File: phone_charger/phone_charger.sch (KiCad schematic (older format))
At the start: 19 parts, among them J1 Conn_01x02, J2 UE27AC54100, U1 ADP2302

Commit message: Place USB on grid; connect shield
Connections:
- wire segments 47 -> 50
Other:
- moved on the sheet: J2
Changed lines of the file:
@@
 L phone_charger-rescue:UE27AC54100-dk_USB-DVI-HDMI-Connectors J2
 U 1 1 5B88DA27
-P 6700 4750
-F 0 "J2" H 6597 4690 60  0000 R CNN
-F 1 "UE27AC54100" H 6597 4796 60  0000 R CNN
-F 2 "phone_charger:USB_A_Female_SS-52100-001" H 6900 4950 60  0001 L CNN
-F 3 "https://www.amphenolcanada.com/ProductSearch/drawings/AC/UE27ACX4X0X.pdf" H 6900 5050 60  0001 L CNN
-F 4 "UE27AC54100-ND" H 6900 5150 60  0001 L CNN "Digi-Key_PN"
-F 5 "UE27AC54100" H 6900 5250 60  0001 L CNN "MPN"
-F 6 "Connectors, Interconnects" H 6900 5350 60  0001 L CNN "Category"
-F 7 "USB, DVI, HDMI Connectors" H 6900 5450 60  0001 L CNN "Family"
-F 8 "https://www.amphenolcanada.com/ProductSearch/drawings/AC/UE27ACX4X0X.pdf" H 6900 5550 60  0001 L CNN "DK_Datasheet_Link"
-F 9 "/product-detail/en/amphenol-commercial-products/UE27AC54100/UE27AC54100-ND/1972253" H 6900 5650 60  0001 L CNN "DK_Detail_Page"
-F 10 "CONN RCPT USB TYPE A R/A GOLD" H 6900 5750 60  0001 L CNN "Description"
-F 11 "Amphenol Commercial Products" H 6900 5850 60  0001 L CNN "Manufacturer"
-F 12 "Active" H 6900 5950 60  0001 L CNN "Status"
-	1    6700 4750
+P 6600 4700
+F 0 "J2" H 6497 4640 60  0000 R CNN
+F 1 "UE27AC54100" H 6497 4746 60  0000 R CNN
+F 2 "phone_charger:USB_A_Female_SS-52100-001" H 6800 4900 60  0001 L CNN
+F 3 "https://www.amphenolcanada.com/ProductSearch/drawings/AC/UE27ACX4X0X.pdf" H 6800 5000 60  0001 L CNN
+F 4 "UE27AC54100-ND" H 6800 5100 60  0001 L CNN "Digi-Key_PN"
+F 5 "UE27AC54100" H 6800 5200 60  0001 L CNN "MPN"
+F 6 "Connectors, Interconnects" H 6800 5300 60  0001 L CNN "Category"
+F 7 "USB, DVI, HDMI Connectors" H 6800 5400 60  0001 L CNN "Family"
+F 8 "https://www.amphenolcanada.com/ProductSearch/drawings/AC/UE27ACX4X0X.pdf" H 6800 5500 60  0001 L CNN "DK_Datasheet_Link"
+F 9 "/product-detail/en/amphenol-commercial-products/UE27AC54100/UE27AC54100-ND/1972253" H 6800 5600 60  0001 L CNN "DK_Detail_Page"
+F 10 "CONN RCPT USB TYPE A R/A GOLD" H 6800 5700 60  0001 L CNN "Description"
+F 11 "Amphenol Commercial Products" H 6800 5800 60  0001 L CNN "Manufacturer"
+F 12 "Active" H 6800 5900 60  0001 L CNN "Status"
+	1    6600 4700
 	-1   0    0    1
 $EndComp
@@
 L phone_charger-rescue:R-Device R3
 U 1 1 5B88DF7C
-P 5500 4000
-F 0 "R3" H 5570 4046 50  0000 L CNN
-F 1 "75k" H 5570 3955 50  0000 L CNN
-F 2 "Resistors_SMD:R_0805_HandSoldering" V 5430 4000 50  0001 C CNN
-F 3 "~" H 5500 4000 50  0001 C CNN
-	1    5500 4000
+P 5400 3950
+F 0 "R3" H 5470 3996 50  0000 L CNN
+F 1 "75k" H 5470 3905 50  0000 L CNN
+F 2 "Resistors_SMD:R_0805_HandSoldering" V 5330 3950 50  0001 C CNN
+F 3 "~" H 5400 3950 50  0001 C CNN
+	1    5400 3950
 	1    0    0    -1
 $EndComp
@@
 L phone_charger-rescue:R-Device R4
 U 1 1 5B88E002
-P 5500 4500
-F 0 "R4" H 5570 4546 50  0000 L CNN
-F 1 "50k" H 5570 4455 50  0000 L CNN
-F 2 "Resistors_SMD:R_0805_HandSoldering" V 5430 4500 50  0001 C CNN
-F 3 "~" H 5500 4500 50  0001 C CNN
-	1    5500 4500
+P 5400 4450
+F 0 "R4" H 5470 4496 50  0000 L CNN
+F 1 "50k" H 5470 4405 50  0000 L CNN
+F 2 "Resistors_SMD:R_0805_HandSoldering" V 5330 4450 50  0001 C CNN
+F 3 "~" H 5400 4450 50  0001 C CNN
+	1    5400 4450
 	1    0    0    -1
 $EndComp
@@
 L phone_charger-rescue:VBUS-power #PWR05
 U 1 1 5B88E11B
-P 5500 3850
-F 0 "#PWR05" H 5500 3700 50  0001 C CNN
-F 1 "VBUS" H 5515 4023 50  0000 C CNN
-F 2 "" H 5500 3850 50  0001 C CNN
-F 3 "" H 5500 3850 50  0001 C CNN
-	1    5500 3850
+P 5400 3800
+F 0 "#PWR05" H 5400 3650 50  0001 C CNN
+F 1 "VBUS" H 5415 3973 50  0000 C CNN
+F 2 "" H 5400 3800 50  0001 C CNN
+F 3 "" H 5400 3800 50  0001 C CNN
+	1    5400 3800
 	1    0    0    -1
 $EndComp
@@
 L phone_charger-rescue:GND-power #PWR06
 U 1 1 5B88E140
-P 5500 4650
-F 0 "#PWR06" H 5500 4400 50  0001 C CNN
-F 1 "GND" H 5505 4477 50  0000 C CNN
-F 2 "" H 5500 4650 50  0001 C CNN
-F 3 "" H 5500 4650 50  0001 C CNN
-	1    5500 4650
+P 5400 4600
+F 0 "#PWR06" H 5400 4350 50  0001 C CNN
+F 1 "GND" H 5405 4427 50  0000 C CNN
+F 2 "" H 5400 4600 50  0001 C CNN
+F 3 "" H 5400 4600 50  0001 C CNN
+	1    5400 4600
 	1    0    0    -1
 $EndComp
@@
 L phone_charger-rescue:R-Device R5
 U 1 1 5B88ED75
-P 5500 5300
-F 0 "R5" H 5570 5346 50  0000 L CNN
-F 1 "43k" H 5570 5255 50  0000 L CNN
-F 2 "Resistors_SMD:R_0603_HandSoldering" V 5430 5300 50  0001 C CNN
-F 3 "~" H 5500 5300 50  0001 C CNN
-	1    5500 5300
+P 5400 5250
+F 0 "R5" H 5470 5296 50  0000 L CNN
+F 1 "43k" H 5470 5205 50  0000 L CNN
+F 2 "Resistors_SMD:R_0603_HandSoldering" V 5330 5250 50  0001 C CNN
+F 3 "~" H 5400 5250 50  0001 C CNN
+	1    5400 5250
 	1    0    0    -1
 $EndComp
@@
 L phone_charger-rescue:R-Device R6
 U 1 1 5B88ED7B
-P 5500 5800
-F 0 "R6" H 5570 5846 50  0000 L CNN
-F 1 "50k" H 5570 5755 50  0000 L CNN
-F 2 "Resistors_SMD:R_0805_HandSoldering" V 5430 5800 50  0001 C CNN
-F 3 "~" H 5500 5800 50  0001 C CNN
-	1    5500 5800
+P 5400 5750
+F 0 "R6" H 5470 5796 50  0000 L CNN
+F 1 "50k" H 5470 5705 50  0000 L CNN
+F 2 "Resistors_SMD:R_0805_HandSoldering" V 5330 5750 50  0001 C CNN
+F 3 "~" H 5400 5750 50  0001 C CNN
+	1    5400 5750
 	1    0    0    -1
 $EndComp
@@
 L phone_charger-rescue:VBUS-power #PWR07
 U 1 1 5B88ED81
-P 5500 5150
-F 0 "#PWR07" H 5500 5000 50  0001 C CNN
-F 1 "VBUS" H 5515 5323 50  0000 C CNN
-F 2 "" H 5500 5150 50  0001 C CNN
-F 3 "" H 5500 5150 50  0001 C CNN
-	1    5500 5150
+P 5400 5100
+F 0 "#PWR07" H 5400 4950 50  0001 C CNN
+F 1 "VBUS" H 5415 5273 50  0000 C CNN
+F 2 "" H 5400 5100 50  0001 C CNN
+F 3 "" H 5400 5100 50  0001 C CNN
+	1    5400 5100
 	1    0    0    -1
 $EndComp
@@
 L phone_charger-rescue:GND-power #PWR08
 U 1 1 5B88ED87
-P 5500 5950
-F 0 "#PWR08" H 5500 5700 50  0001 C CNN
-F 1 "GND" H 5505 5777 50  0000 C CNN
-F 2 "" H 5500 5950 50  0001 C CNN
-F 3 "" H 5500 5950 50  0001 C CNN
-	1    5500 5950
+P 5400 5900
+F 0 "#PWR08" H 5400 5650 50  0001 C CNN
+F 1 "GND" H 5405 5727 50  0000 C CNN
+F 2 "" H 5400 5900 50  0001 C CNN
+F 3 "" H 5400 5900 50  0001 C CNN
+	1    5400 5900
 	1    0    0    -1
 $EndComp
@@
 L phone_charger-rescue:R-Device R7
 U 1 1 5B88F6A0
-P 5800 4800
-F 0 "R7" H 5850 5100 50  0000 L CNN
-F 1 "0R (OPT)" H 5850 5000 50  0000 L CNN
-F 2 "Resistors_SMD:R_0603_HandSoldering" V 5730 4800 50  0001 C CNN
-F 3 "~" H 5800 4800 50  0001 C CNN
-	1    5800 4800
-	1    0    0    -1
-$EndComp
-Wire Wire Line
-	5800 4250 5800 4650
-Connection ~ 5800 4650
-Wire Wire Line
-	5800 5550 5800 4950
-Connection ~ 5800 4950
-Wire Wire Line
-	5500 4150 5500 4250
-Wire Wire Line
-	5500 5450 5500 5550
-Wire Wire Line
-	5800 4250 5500 4250
-Connection ~ 5500 4250
-Wire Wire Line
-	5500 4250 5500 4350
-Wire Wire Line
-	5800 5550 5500 5550
-Connection ~ 5500 5550
-Wire Wire Line
-	5500 5550 5500 5650
+P 5700 4750
+F 0 "R7" H 5750 5050 50  0000 L CNN
+F 1 "0R (OPT)" H 5750 4950 50  0000 L CNN
+F 2 "Resistors_SMD:R_0603_HandSoldering" V 5630 4750 50  0001 C CNN
+F 3 "~" H 5700 4750 50  0001 C CNN
+	1    5700 4750
+	1    0    0    -1
+$EndComp
+Wire Wire Line
+	5700 4200 5700 4600
+Connection ~ 5700 4600
+Wire Wire Line
+	5700 5500 5700 4900
+Connection ~ 5700 4900
+Wire Wire Line
+	5400 4100 5400 4200
+Wire Wire Line
+	5400 5400 5400 5500
+Wire Wire Line
+	5700 4200 5400 4200
+Connection ~ 5400 4200
+Wire Wire Line
+	5400 4200 5400 4300
+Wire Wire Line
+	5700 5500 5400 5500
+Connection ~ 5400 5500
+Wire Wire Line
+	5400 5500 5400 5600
 $Comp
 L phone_charger-rescue:GND-power #PWR011
 U 1 1 5B89256C
-P 6300 5950
-F 0 "#PWR011" H 6300 5700 50  0001 C CNN
-F 1 "GND" H 6305 5777 50  0000 C CNN
-F 2 "" H 6300 5950 50  0001 C CNN
-F 3 "" H 6300 5950 50  0001 C CNN
-	1    6300 5950
-	1    0    0    -1
-$EndComp
-Wire Wire Line
-	6400 4950 6300 4950
+P 6200 5900
+F 0 "#PWR011" H 6200 5650 50  0001 C CNN
+F 1 "GND" H 6205 5727 50  0000 C CNN
+F 2 "" H 6200 5900 50  0001 C CNN
+F 3 "" H 6200 5900 50  0001 C CNN
+	1    6200 5900
+	1    0    0    -1
+$EndComp
+Wire Wire Line
+	6300 4900 6200 4900
 $Comp
 L phone_charger-rescue:VBUS-power #PWR010
 U 1 1 5B892D7D
-P 6300 3850
-F 0 "#PWR010" H 6300 3700 50  0001 C CNN
-F 1 "VBUS" H 6315 4023 50  0000 C CNN
-F 2 "" H 6300 3850 50  0001 C CNN
-F 3 "" H 6300 3850 50  0001 C CNN
-	1    6300 3850
-	1    0    0    -1
-$EndComp
-Wire Wire Line
-	6300 3850 6300 4650
-Wire Wire Line
-	6300 4650 6400 4650
+P 6200 3800
+F 0 "#PWR010" H 6200 3650 50  0001 C CNN
+F 1 "VBUS" H 6215 3973 50  0000 C CNN
+F 2 "" H 6200 3800 50  0001 C CNN
+F 3 "" H 6200 3800 50  0001 C CNN
+	1    6200 3800
+	1    0    0    -1
+$EndComp
+Wire Wire Line
+	6200 3800 6200 4600
+Wire Wire Line
+	6200 4600 6300 4600
 $Comp
 L phone_charger-rescue:Polyfuse-Device F1
@@
 Wire Wire Line
 	8400 1950 8400 1150
-Text Label 6250 4750 0    50   ~ 0
+Text Label 6150 4700 0    50   ~ 0
 D-
-Text Label 6250 4850 0    50   ~ 0
+Text Label 6150 4800 0    50   ~ 0
 D+
 Text Notes 4700 6350 0    50   ~ 0
 Populate EITHER Apple divider resistors or 200 ohm short.
 Wire Wire Line
-	6100 4750 6100 4650
-Wire Wire Line
-	6100 4750 6400 4750
-Wire Wire Line
-	5800 4650 6100 4650
-Wire Wire Line
-	6100 4850 6100 4950
-Wire Wire Line
-	6100 4850 6400 4850
-Wire Wire Line
-	5800 4950 6100 4950
+	6000 4700 6000 4600
+Wire Wire Line
+	6000 4700 6300 4700
+Wire Wire Line
+	5700 4600 6000 4600
+Wire Wire Line
+	6000 4800 6000 4900
+Wire Wire Line
+	6000 4800 6300 4800
+Wire Wire Line
+	5700 4900 6000 4900
 $Comp
 L phone_charger-rescue:ADP2302 U1
@@
 $EndComp
 Wire Wire Line
-	6300 4950 6300 5950
+	6200 4900 6200 5200
+Wire Wire Line
+	6500 5100 6500 5200
+Wire Wire Line
+	6500 5200 6200 5200
+Connection ~ 6200 5200
+Wire Wire Line
+	6200 5200 6200 5900
 $EndSCHEMATC

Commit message: Point to footprint in our library
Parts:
- D2: footprint Diodes_SMD:D_SOD-123 -> phone_charger:D_SOD-123
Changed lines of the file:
@@
 F 0 "D2" H 3550 1384 50  0000 C CNN
 F 1 "D_Schottky" H 3550 1475 50  0000 C CNN
-F 2 "Diodes_SMD:D_SOD-123" H 3550 1600 50  0001 C CNN
+F 2 "phone_charger:D_SOD-123" H 3550 1600 50  0001 C CNN
 F 3 "~" H 3550 1600 50  0001 C CNN
 	1    3550 1600

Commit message: Use smaller THT resistor
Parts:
- R1: footprint Resistors_THT:R_Axial_DIN0309_L9.0mm_D3.2mm_P12.70mm_Horizontal -> Resistor_THT:R_Axial_DIN0207_L6.3mm_D2.5mm_P10.16mm_Horizontal
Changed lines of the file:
@@
 F 0 "R1" H 3070 4596 50  0000 L CNN
 F 1 "300R" H 3070 4505 50  0000 L CNN
-F 2 "Resistors_THT:R_Axial_DIN0309_L9.0mm_D3.2mm_P12.70mm_Horizontal" V 2930 4550 50  0001 C CNN
+F 2 "Resistor_THT:R_Axial_DIN0207_L6.3mm_D2.5mm_P10.16mm_Horizontal" V 2930 4550 50  0001 C CNN
 F 3 "~" H 3000 4550 50  0001 C CNN
 	1    3000 4550

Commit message: Updated header footprint for charger layout
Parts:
- J1: footprint Pin_Headers:Pin_Header_Straight_1x02_Pitch1.00mm -> Pin_Headers:Pin_Header_Straight_1x02_Pitch2.54mm
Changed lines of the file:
@@
 F 0 "J1" H 2120 1817 50  0000 C CNN
 F 1 "Conn_01x02" H 2120 1726 50  0000 C CNN
-F 2 "Pin_Headers:Pin_Header_Straight_1x02_Pitch1.00mm" H 2200 1600 50  0001 C CNN
+F 2 "Pin_Headers:Pin_Header_Straight_1x02_Pitch2.54mm" H 2200 1600 50  0001 C CNN
 F 3 "~" H 2200 1600 50  0001 C CNN
 	1    2200 1600

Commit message: Label switch node
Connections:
- net labels added: SWN
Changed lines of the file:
@@
 Wire Wire Line
 	6200 5200 6200 5900
+Text Label 6950 1950 0    50   ~ 0
+SWN
 $EndSCHEMATC

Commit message: Remap Device libraries and remove unused symbols
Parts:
- C1, C2, C3, C4: symbol phone_charger-rescue:C-device -> Device:C
- D3: symbol phone_charger-rescue:D_Schottky-device -> Device:D_Schottky
- F1: symbol phone_charger-rescue:Polyfuse-Device -> Device:Polyfuse
- L1: symbol phone_charger-rescue:L-device -> Device:L
- R2: symbol phone_charger-rescue:R-device -> Device:R
- R3, R4, R5, R6, R7: symbol phone_charger-rescue:R-Device -> Device:R
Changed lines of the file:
@@
 $EndDescr
 $Comp
-L phone_charger-rescue:L-device L1
+L Device:L L1
 U 1 1 5B85F10E
 P 7250 1950
@@
 $EndComp
 $Comp
-L phone_charger-rescue:C-device C4
+L Device:C C4
 U 1 1 5B85F280
 P 8000 2150
@@
 $EndComp
 $Comp
-L phone_charger-rescue:D_Schottky-device D3
+L Device:D_Schottky D3
 U 1 1 5B861A87
 P 6900 2100
@@
 $EndComp
 $Comp
-L phone_charger-rescue:C-device C2
+L Device:C C2
 U 1 1 5B86257D
 P 6900 1750
@@
 $EndComp
 $Comp
-L phone_charger-rescue:C-device C1
+L Device:C C1
 U 1 1 5B8626AF
 P 4700 1750
@@
 	6900 1950 7100 1950
 $Comp
-L phone_charger-rescue:R-device R2
+L Device:R R2
 U 1 1 5B863BFA
 P 5350 2100
@@
 $EndComp
 $Comp
-L phone_charger-rescue:R-Device R3
+L Device:R R3
 U 1 1 5B88DF7C
 P 5400 3950
@@
 $EndComp
 $Comp
-L phone_charger-rescue:R-Device R4
+L Device:R R4
 U 1 1 5B88E002
 P 5400 4450
@@
 $EndComp
 $Comp
-L phone_charger-rescue:R-Device R5
+L Device:R R5
 U 1 1 5B88ED75
 P 5400 5250
@@
 $EndComp
 $Comp
-L phone_charger-rescue:R-Device R6
+L Device:R R6
 U 1 1 5B88ED7B
 P 5400 5750
@@
 $EndComp
 $Comp
-L phone_charger-rescue:R-Device R7
+L Device:R R7
 U 1 1 5B88F6A0
 P 5700 4750
@@
 	6200 4600 6300 4600
 $Comp
-L phone_charger-rescue:Polyfuse-Device F1
+L Device:Polyfuse F1
 U 1 1 5B8946FD
 P 2850 1600
@@
 	7400 1950 7550 1950
 $Comp
-L phone_charger-rescue:C-device C3
+L Device:C C3
 U 1 1 5BA0CE0C
 P 7550 2150

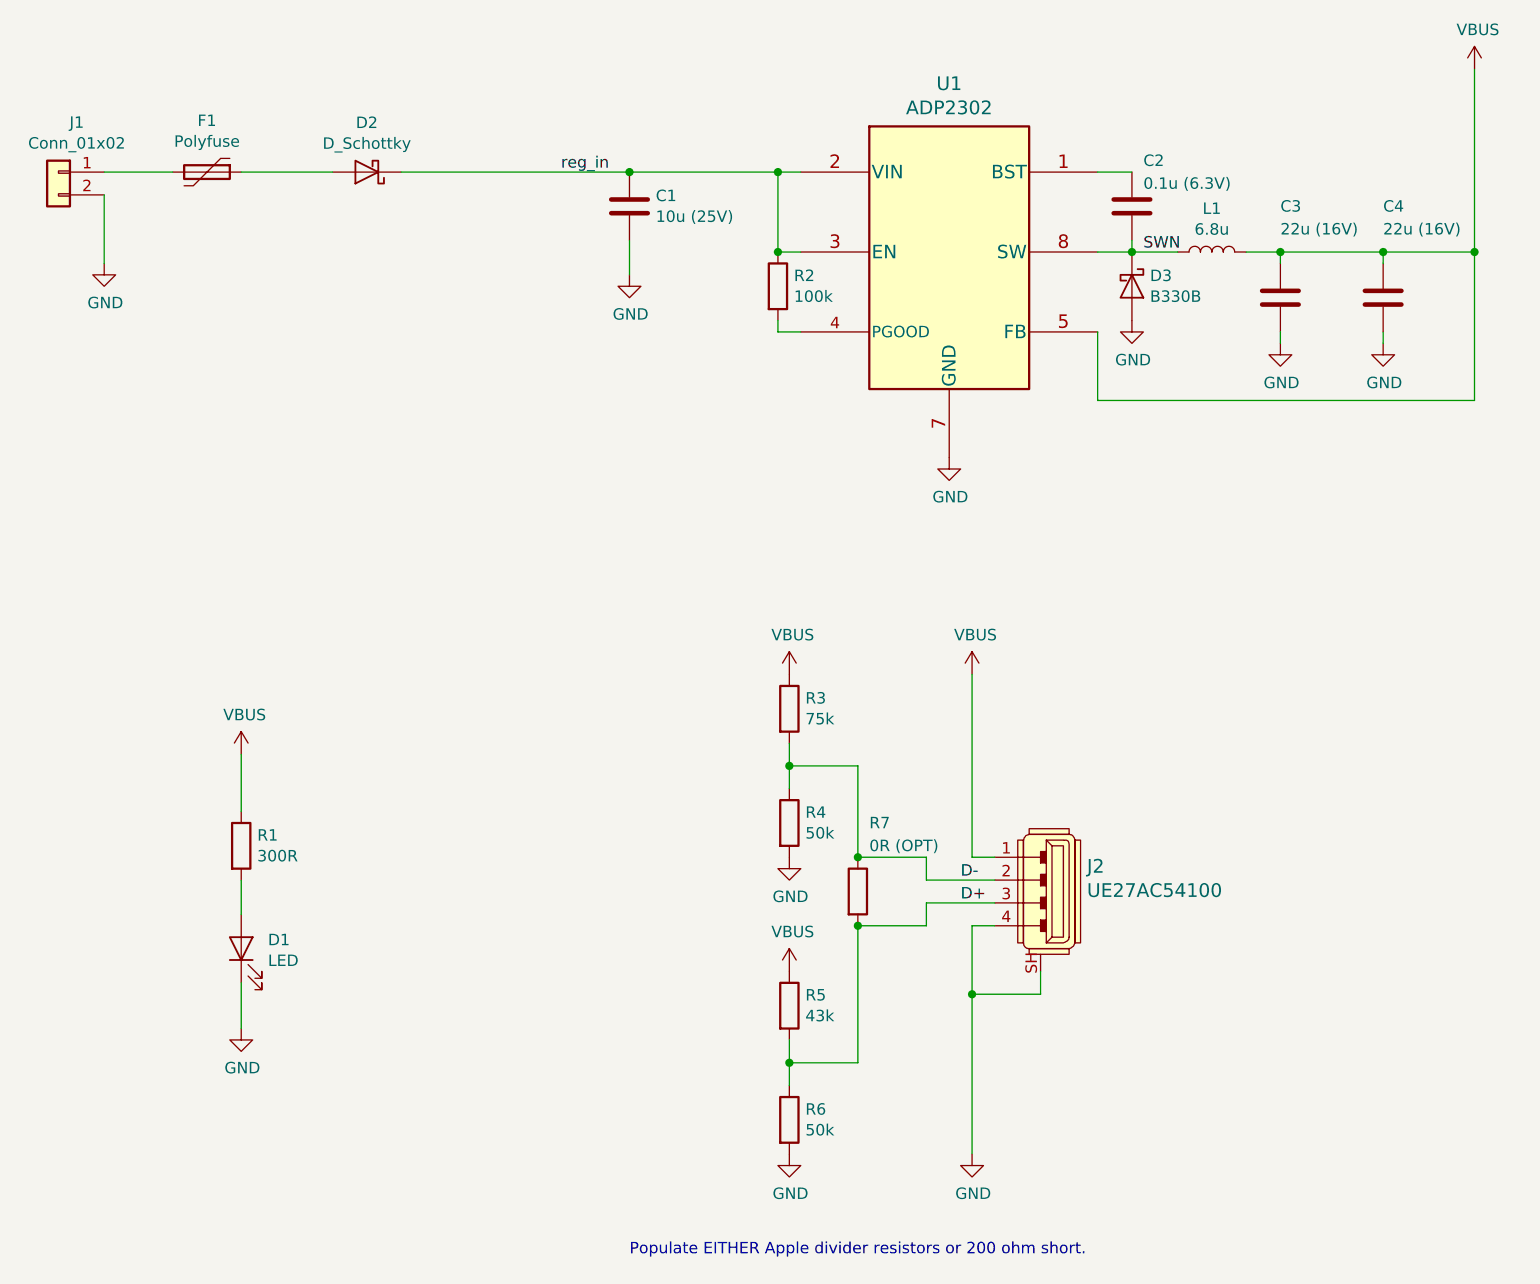
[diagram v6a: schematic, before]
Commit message: Add datasheet links
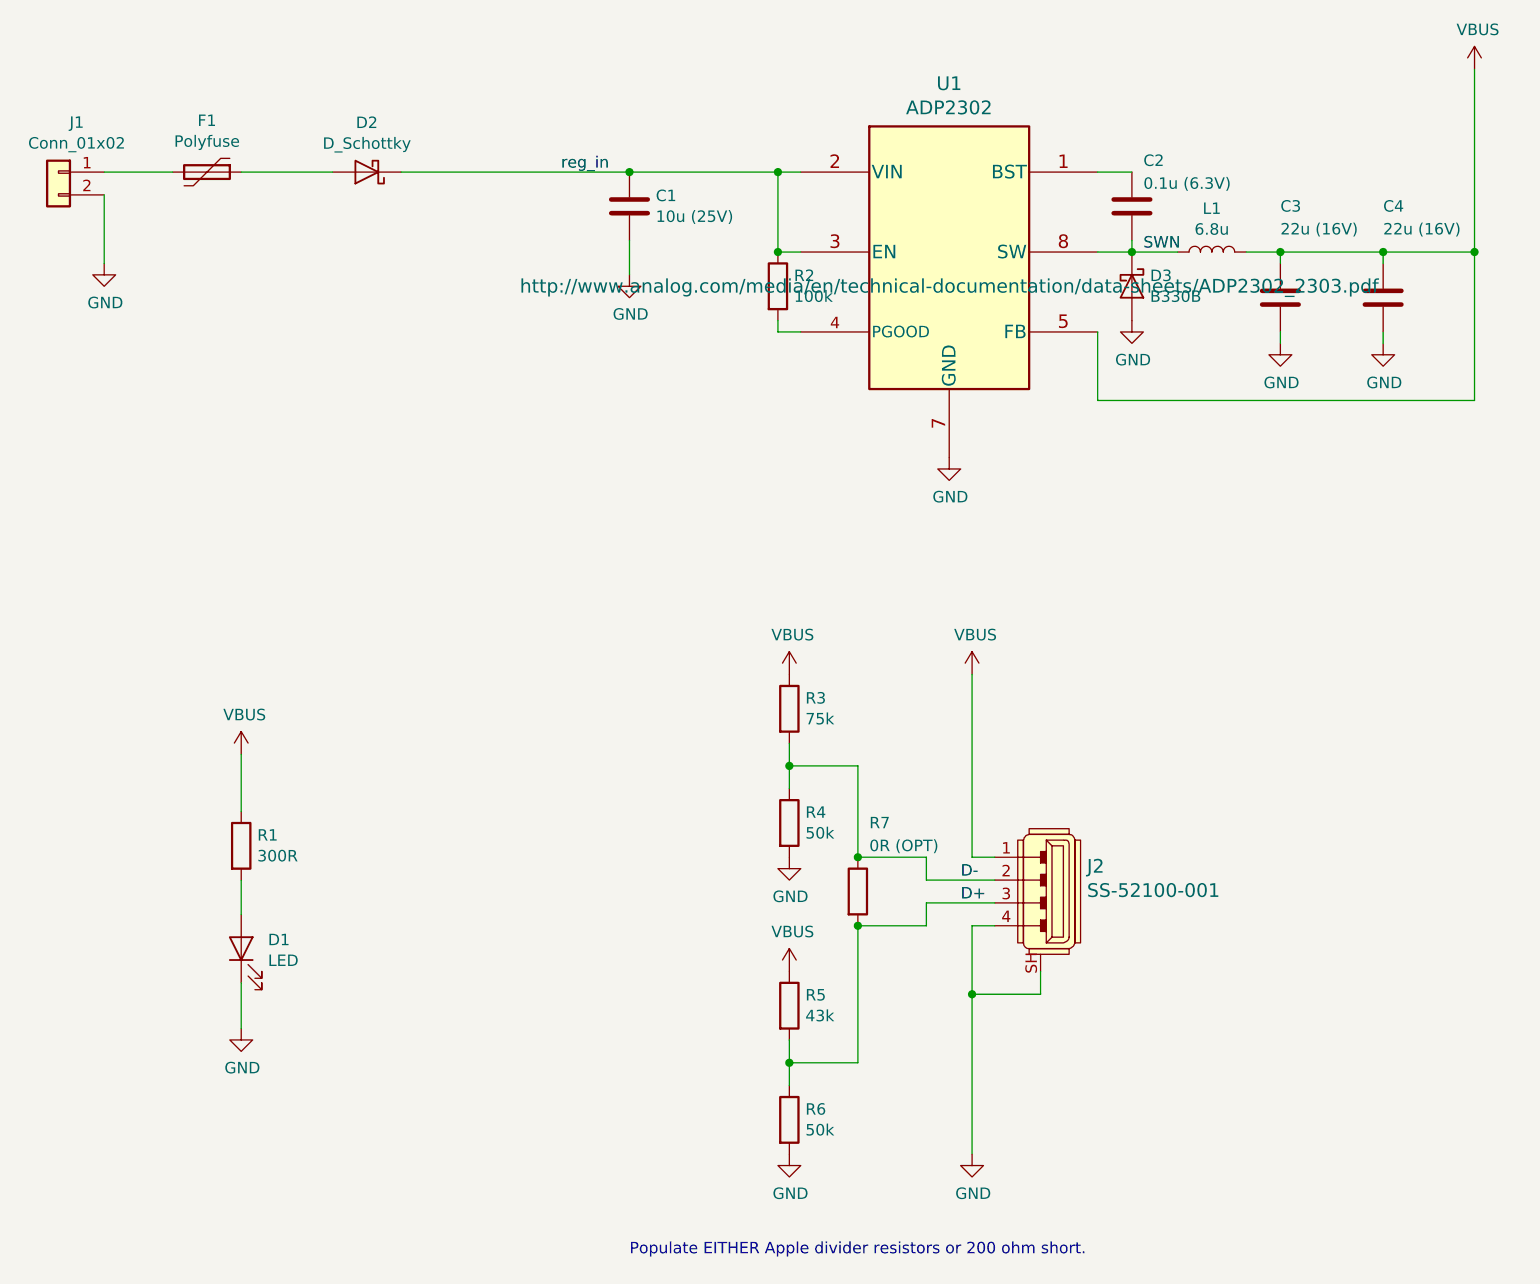
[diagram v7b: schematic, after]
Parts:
- J2: value UE27AC54100 -> SS-52100-001
- U1: Digi-Key_PN (none) -> 584-ADP2302ARDZ-R7
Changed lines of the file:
@@
 P 6600 4700
 F 0 "J2" H 6497 4640 60  0000 R CNN
-F 1 "UE27AC54100" H 6497 4746 60  0000 R CNN
+F 1 "SS-52100-001" H 6497 4746 60  0000 R CNN
 F 2 "phone_charger:USB_A_Female_SS-52100-001" H 6800 4900 60  0001 L CNN
 F 3 "https://www.amphenolcanada.com/ProductSearch/drawings/AC/UE27ACX4X0X.pdf" H 6800 5000 60  0001 L CNN
@@
 F 1 "ADP2302" H 6100 2581 60  0000 C CNN
 F 2 "Housings_SOIC:SOIC-8-1EP_3.9x4.9mm_Pitch1.27mm" H 6100 2600 60  0001 C CNN
-F 3 "" H 6100 1800 60  0000 C CNN
+F 3 "http://www.analog.com/media/en/technical-documentation/data-sheets/ADP2302_2303.pdf" H 6100 1800 60  0000 C CNN
+F 4 "584-ADP2302ARDZ-R7" H 6100 1950 50  0001 C CNN "Digi-Key_PN"
 	1    6100 1950
 	1    0    0    -1
